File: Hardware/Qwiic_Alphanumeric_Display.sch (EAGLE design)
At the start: 33 parts, among them J4 Vertical Qwiic Connector, J5 Vertical Qwiic Connector, U2 XC9140

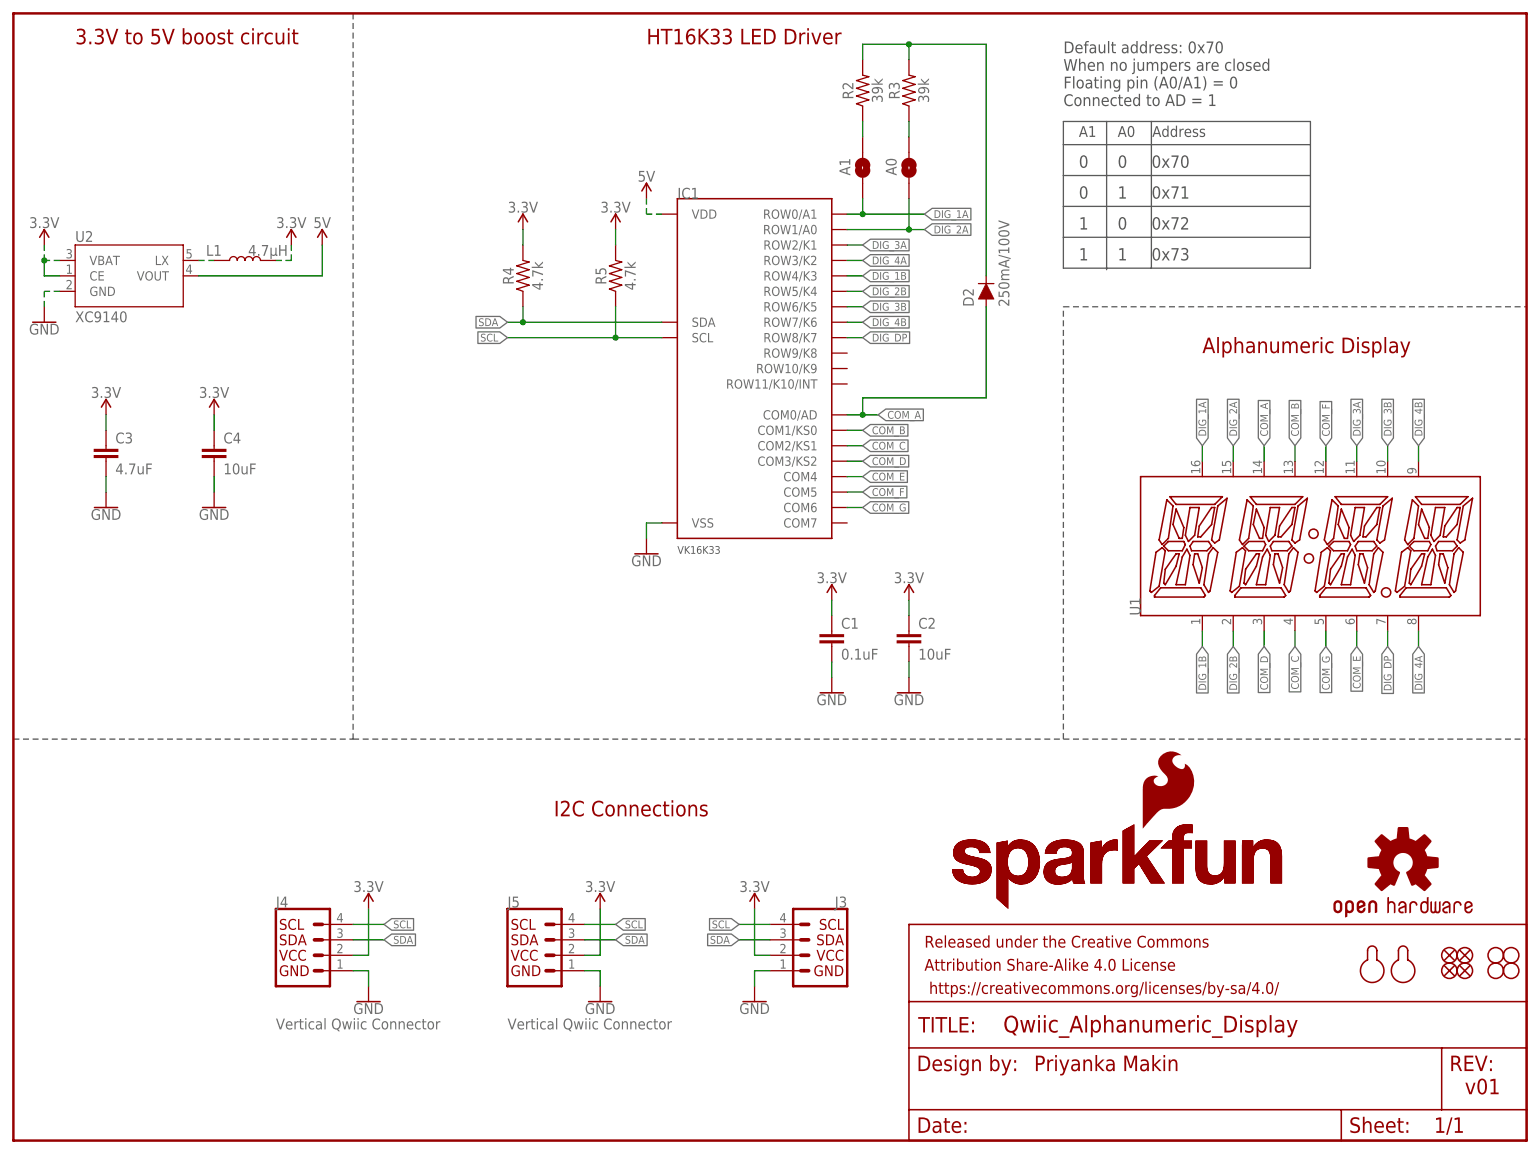
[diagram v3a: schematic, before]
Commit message: Run checklist
Add voltage ranges on schematic
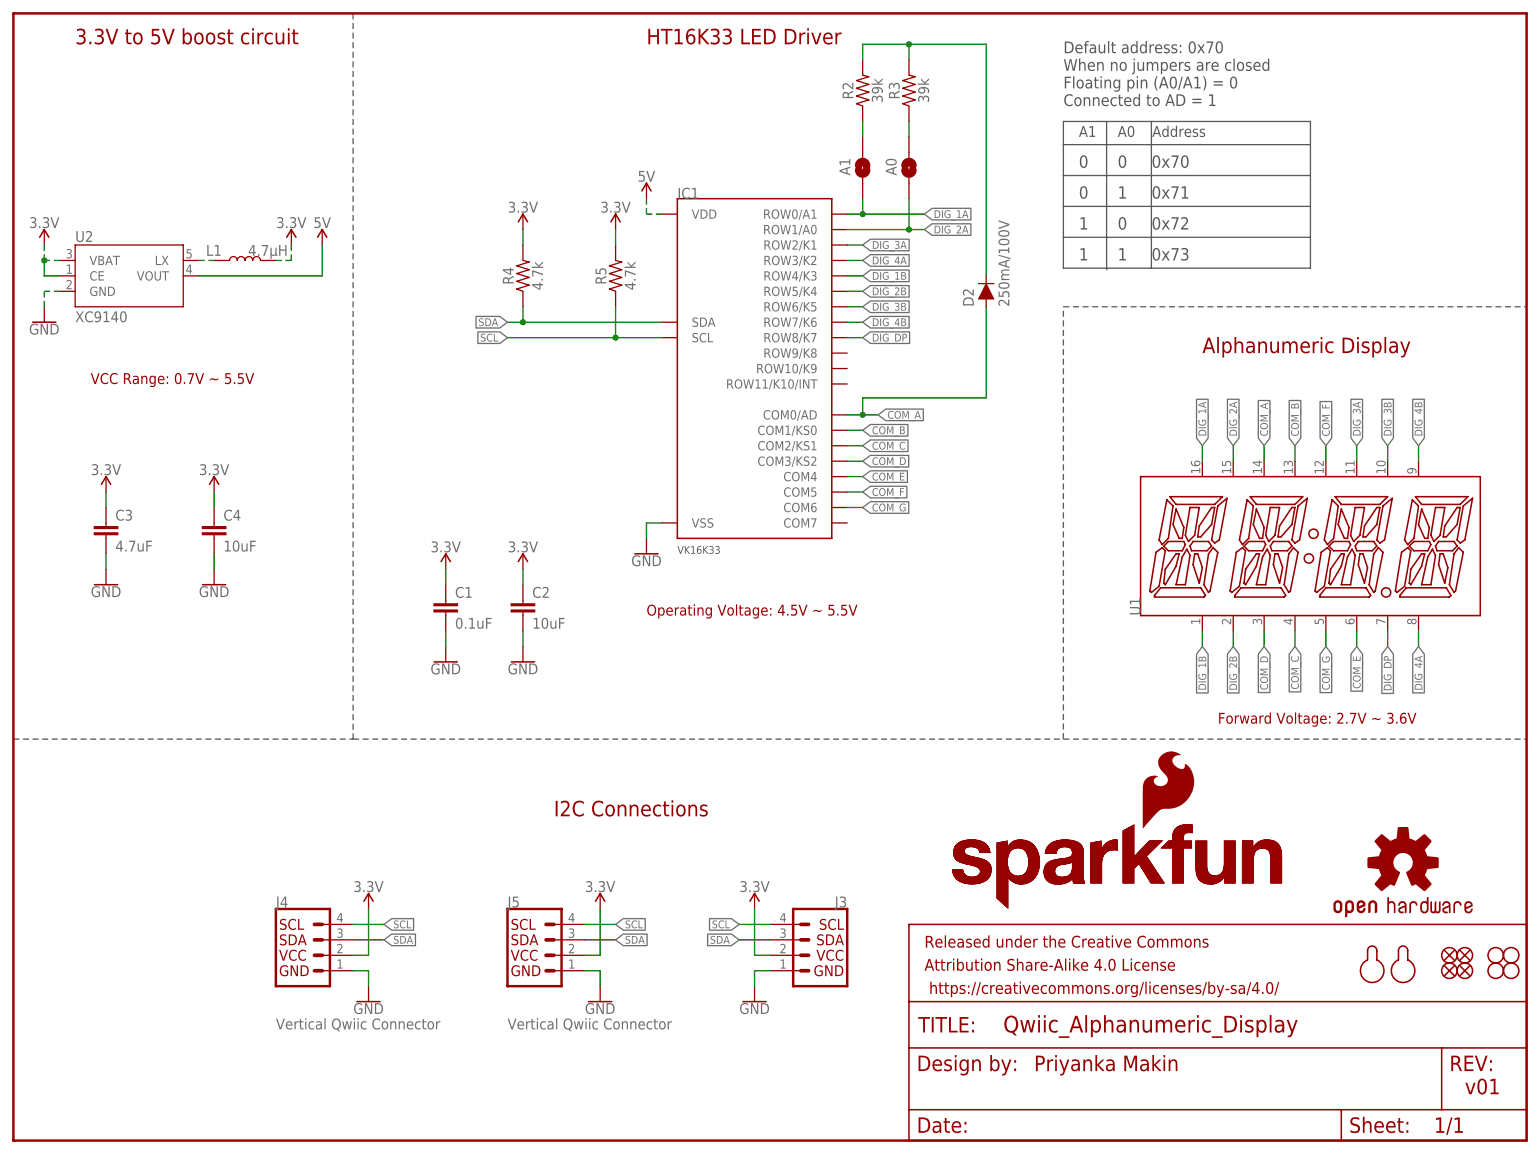
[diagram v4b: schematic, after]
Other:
- note added: "Forward Voltage: 2.7V ~ 3.6V"
- note added: "Operating Voltage: 4.5V ~ 5.5V"
- note added: "VCC Range: 0.7V ~ 5.5V"
- moved on the sheet: C1, C2, C3, C4
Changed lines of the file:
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@@
 <text x="10.16" y="180.34" size="2.54" layer="94" font="vector">3.3V to 5V boost circuit</text>
 <text x="109.22" y="96.52" size="1.27" layer="97" font="vector">VK16K33</text>
+<text x="12.7" y="124.46" size="1.778" layer="94" font="vector">VCC Range: 0.7V ~ 5.5V</text>
+<text x="104.14" y="86.36" size="1.778" layer="94" font="vector">Operating Voltage: 4.5V ~ 5.5V</text>
+<text x="198.12" y="68.58" size="1.778" layer="94" font="vector">Forward Voltage: 2.7V ~ 3.6V</text>
 </plain>
 <instances>
@@
 <attribute name="NAME" x="137.16" y="38.354" size="1.778" layer="95" font="vector" rot="MR0"/>
 </instance>
-<instance part="GND2" gate="1" x="134.62" y="73.66" smashed="yes">
-<attribute name="VALUE" x="134.62" y="73.406" size="1.778" layer="96" font="vector" align="top-center"/>
-</instance>
-<instance part="C1" gate="G$1" x="134.62" y="81.28" smashed="yes">
-<attribute name="NAME" x="136.144" y="84.201" size="1.778" layer="95" font="vector"/>
-<attribute name="VALUE" x="136.144" y="79.121" size="1.778" layer="96" font="vector"/>
-</instance>
-<instance part="SUPPLY2" gate="G$1" x="134.62" y="88.9" smashed="yes">
-<attribute name="VALUE" x="134.62" y="91.694" size="1.778" layer="96" font="vector" align="bottom-center"/>
+<instance part="GND2" gate="1" x="71.12" y="78.74" smashed="yes">
+<attribute name="VALUE" x="71.12" y="78.486" size="1.778" layer="96" font="vector" align="top-center"/>
+</instance>
+<instance part="C1" gate="G$1" x="71.12" y="86.36" smashed="yes">
+<attribute name="NAME" x="72.644" y="89.281" size="1.778" layer="95" font="vector"/>
+<attribute name="VALUE" x="72.644" y="84.201" size="1.778" layer="96" font="vector"/>
+</instance>
+<instance part="SUPPLY2" gate="G$1" x="71.12" y="93.98" smashed="yes">
+<attribute name="VALUE" x="71.12" y="96.774" size="1.778" layer="96" font="vector" align="bottom-center"/>
 </instance>
 <instance part="SUPPLY4" gate="G$1" x="121.92" y="38.1" smashed="yes" rot="MR0">
@@
 <instance part="H3" gate="G$1" x="246.38" y="30.48" smashed="yes"/>
 <instance part="H4" gate="G$1" x="246.38" y="27.94" smashed="yes"/>
-<instance part="GND3" gate="1" x="147.32" y="73.66" smashed="yes">
-<attribute name="VALUE" x="147.32" y="73.406" size="1.778" layer="96" font="vector" align="top-center"/>
-</instance>
-<instance part="C2" gate="G$1" x="147.32" y="81.28" smashed="yes">
-<attribute name="NAME" x="148.844" y="84.201" size="1.778" layer="95" font="vector"/>
-<attribute name="VALUE" x="148.844" y="79.121" size="1.778" layer="96" font="vector"/>
-</instance>
-<instance part="SUPPLY3" gate="G$1" x="147.32" y="88.9" smashed="yes">
-<attribute name="VALUE" x="147.32" y="91.694" size="1.778" layer="96" font="vector" align="bottom-center"/>
+<instance part="GND3" gate="1" x="83.82" y="78.74" smashed="yes">
+<attribute name="VALUE" x="83.82" y="78.486" size="1.778" layer="96" font="vector" align="top-center"/>
+</instance>
+<instance part="C2" gate="G$1" x="83.82" y="86.36" smashed="yes">
+<attribute name="NAME" x="85.344" y="89.281" size="1.778" layer="95" font="vector"/>
+<attribute name="VALUE" x="85.344" y="84.201" size="1.778" layer="96" font="vector"/>
+</instance>
+<instance part="SUPPLY3" gate="G$1" x="83.82" y="93.98" smashed="yes">
+<attribute name="VALUE" x="83.82" y="96.774" size="1.778" layer="96" font="vector" align="bottom-center"/>
 </instance>
 <instance part="U2" gate="U1" x="17.78" y="142.24" smashed="yes">
@@
 <attribute name="VALUE" x="5.08" y="134.366" size="1.778" layer="96" font="vector" align="top-center"/>
 </instance>
-<instance part="C3" gate="G$1" x="15.24" y="111.76" smashed="yes">
-<attribute name="NAME" x="16.764" y="114.681" size="1.778" layer="95" font="vector"/>
-<attribute name="VALUE" x="16.764" y="109.601" size="1.778" layer="96" font="vector"/>
-</instance>
-<instance part="C4" gate="G$1" x="33.02" y="111.76" smashed="yes">
-<attribute name="NAME" x="34.544" y="114.681" size="1.778" layer="95" font="vector"/>
-<attribute name="VALUE" x="34.544" y="109.601" size="1.778" layer="96" font="vector"/>
-</instance>
-<instance part="GND9" gate="1" x="15.24" y="104.14" smashed="yes">
-<attribute name="VALUE" x="15.24" y="103.886" size="1.778" layer="96" font="vector" align="top-center"/>
-</instance>
-<instance part="GND10" gate="1" x="33.02" y="104.14" smashed="yes">
-<attribute name="VALUE" x="33.02" y="103.886" size="1.778" layer="96" font="vector" align="top-center"/>
-</instance>
-<instance part="SUPPLY10" gate="G$1" x="15.24" y="119.38" smashed="yes">
-<attribute name="VALUE" x="15.24" y="122.174" size="1.778" layer="96" font="vector" align="bottom-center"/>
-</instance>
-<instance part="SUPPLY11" gate="G$1" x="33.02" y="119.38" smashed="yes">
-<attribute name="VALUE" x="33.02" y="122.174" size="1.778" layer="96" font="vector" align="bottom-center"/>
+<instance part="C3" gate="G$1" x="15.24" y="99.06" smashed="yes">
+<attribute name="NAME" x="16.764" y="101.981" size="1.778" layer="95" font="vector"/>
+<attribute name="VALUE" x="16.764" y="96.901" size="1.778" layer="96" font="vector"/>
+</instance>
+<instance part="C4" gate="G$1" x="33.02" y="99.06" smashed="yes">
+<attribute name="NAME" x="34.544" y="101.981" size="1.778" layer="95" font="vector"/>
+<attribute name="VALUE" x="34.544" y="96.901" size="1.778" layer="96" font="vector"/>
+</instance>
+<instance part="GND9" gate="1" x="15.24" y="91.44" smashed="yes">
+<attribute name="VALUE" x="15.24" y="91.186" size="1.778" layer="96" font="vector" align="top-center"/>
+</instance>
+<instance part="GND10" gate="1" x="33.02" y="91.44" smashed="yes">
+<attribute name="VALUE" x="33.02" y="91.186" size="1.778" layer="96" font="vector" align="top-center"/>
+</instance>
+<instance part="SUPPLY10" gate="G$1" x="15.24" y="106.68" smashed="yes">
+<attribute name="VALUE" x="15.24" y="109.474" size="1.778" layer="96" font="vector" align="bottom-center"/>
+</instance>
+<instance part="SUPPLY11" gate="G$1" x="33.02" y="106.68" smashed="yes">
+<attribute name="VALUE" x="33.02" y="109.474" size="1.778" layer="96" font="vector" align="bottom-center"/>
 </instance>
 <instance part="L1" gate="G$1" x="38.1" y="144.78" smashed="yes" rot="R90">
@@
 <pinref part="C1" gate="G$1" pin="1"/>
 <pinref part="SUPPLY2" gate="G$1" pin="3.3V"/>
-<wire x1="134.62" y1="86.36" x2="134.62" y2="88.9" width="0.1524" layer="91"/>
+<wire x1="71.12" y1="91.44" x2="71.12" y2="93.98" width="0.1524" layer="91"/>
 </segment>
 <segment>
@@
 <pinref part="C2" gate="G$1" pin="1"/>
 <pinref part="SUPPLY3" gate="G$1" pin="3.3V"/>
-<wire x1="147.32" y1="86.36" x2="147.32" y2="88.9" width="0.1524" layer="91"/>
+<wire x1="83.82" y1="91.44" x2="83.82" y2="93.98" width="0.1524" layer="91"/>
 </segment>
 <segment>
 <pinref part="C3" gate="G$1" pin="1"/>
 <pinref part="SUPPLY10" gate="G$1" pin="3.3V"/>
-<wire x1="15.24" y1="119.38" x2="15.24" y2="116.84" width="0.1524" layer="91"/>
+<wire x1="15.24" y1="106.68" x2="15.24" y2="104.14" width="0.1524" layer="91"/>
 </segment>
 <segment>
 <pinref part="C4" gate="G$1" pin="1"/>
 <pinref part="SUPPLY11" gate="G$1" pin="3.3V"/>
-<wire x1="33.02" y1="119.38" x2="33.02" y2="116.84" width="0.1524" layer="91"/>
+<wire x1="33.02" y1="106.68" x2="33.02" y2="104.14" width="0.1524" layer="91"/>
 </segment>
 <segment>
@@
 <pinref part="GND2" gate="1" pin="GND"/>
 <pinref part="C1" gate="G$1" pin="2"/>
-<wire x1="134.62" y1="76.2" x2="134.62" y2="78.74" width="0.1524" layer="91"/>
+<wire x1="71.12" y1="81.28" x2="71.12" y2="83.82" width="0.1524" layer="91"/>
 </segment>
 <segment>
@@
 <pinref part="GND3" gate="1" pin="GND"/>
 <pinref part="C2" gate="G$1" pin="2"/>
-<wire x1="147.32" y1="76.2" x2="147.32" y2="78.74" width="0.1524" layer="91"/>
+<wire x1="83.82" y1="81.28" x2="83.82" y2="83.82" width="0.1524" layer="91"/>
 </segment>
 <segment>
 <pinref part="C3" gate="G$1" pin="2"/>
 <pinref part="GND9" gate="1" pin="GND"/>
-<wire x1="15.24" y1="106.68" x2="15.24" y2="109.22" width="0.1524" layer="91"/>
+<wire x1="15.24" y1="93.98" x2="15.24" y2="96.52" width="0.1524" layer="91"/>
 </segment>
 <segment>
 <pinref part="C4" gate="G$1" pin="2"/>
 <pinref part="GND10" gate="1" pin="GND"/>
-<wire x1="33.02" y1="106.68" x2="33.02" y2="109.22" width="0.1524" layer="91"/>
-</segment>
-<segment>
+<wire x1="33.02" y1="93.98" x2="33.02" y2="96.52" width="0.1524" layer="91"/>
+</segment>
+<segment>
